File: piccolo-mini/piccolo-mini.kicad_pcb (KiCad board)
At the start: 2 copper layers, 96.1 x 20.6 mm, 16 parts, among them SW1 SW_Push, U1 ProMicro

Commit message: Continued tweaks
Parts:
- D1, D2, D3, D4, D5: footprint Keebio-Parts:Diode-Hybrid-Back -> Envoy:Diode-Hybrid-Back; moved to B.Cu
- MX1, MX2, MX3, MX4, MX5: footprint kbd:CherryMX_Hotswap -> Envoy:MXOnly-1U-Hotswap
- RESET1: renamed from SW1; footprint kbd:ResetSW -> Envoy:Reset_Jumper_Points
- U1: footprint Envoy:ProMicro_v3 -> Envoy:ProMicro_face_out; moved to B.Cu
- moved D3 3.12 mm to (192.4, 86.3)
- moved U1 1.00 mm to (151.7, 88.8), turned to -90 degrees
- moved D1 0.60 mm to (152.4, 88.2)
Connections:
- U1 pad 1: Net-(U1-Pad1) -> unconnected-(U1-Pad1)
- U1 pad 11: Net-(U1-Pad11) -> unconnected-(U1-Pad11)
- U1 pad 16: Net-(U1-Pad16) -> unconnected-(U1-Pad16)
- U1 pad 17: Net-(U1-Pad17) -> unconnected-(U1-Pad17)
- U1 pad 18: Net-(U1-Pad18) -> unconnected-(U1-Pad18)
- U1 pad 19: Net-(U1-Pad19) -> unconnected-(U1-Pad19)
- U1 pad 2: Net-(U1-Pad2) -> unconnected-(U1-Pad2)
- U1 pad 20: Net-(U1-Pad20) -> unconnected-(U1-Pad20)
- U1 pad 24: Net-(U1-Pad24) -> unconnected-(U1-Pad24)
- U1 pad 5: Net-(U1-Pad5) -> unconnected-(U1-Pad5)
- U1 pad 6: Net-(U1-Pad6) -> unconnected-(U1-Pad6)
- U1 pad 7: Net-(U1-Pad7) -> unconnected-(U1-Pad7)
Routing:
- net col0: track 63.5 -> 72.6 mm
- net GND: track 101.6 -> 107.7 mm
- net row0: track 40.8 -> 44.3 mm
- net row1: track 67.5 -> 70.9 mm, vias 2 -> 1
- net col2: track 19.2 -> 17.1 mm
- net Net-(D3-Pad2): track 3.38 -> 5.30 mm
- net col1: track 73.9 -> 74.9 mm
- net EncoderA: track 53.9 -> 54.6 mm
- net Reset: track 36.6 -> 37.2 mm
- net EncoderB: track 63.0 -> 62.6 mm, vias 2 -> 0
- added copper zone on B.Cu, net GND
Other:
- board size 96.1 x 20.6 mm -> 96.9 x 20.6 mm
- net class Default removed
- net class Power removed

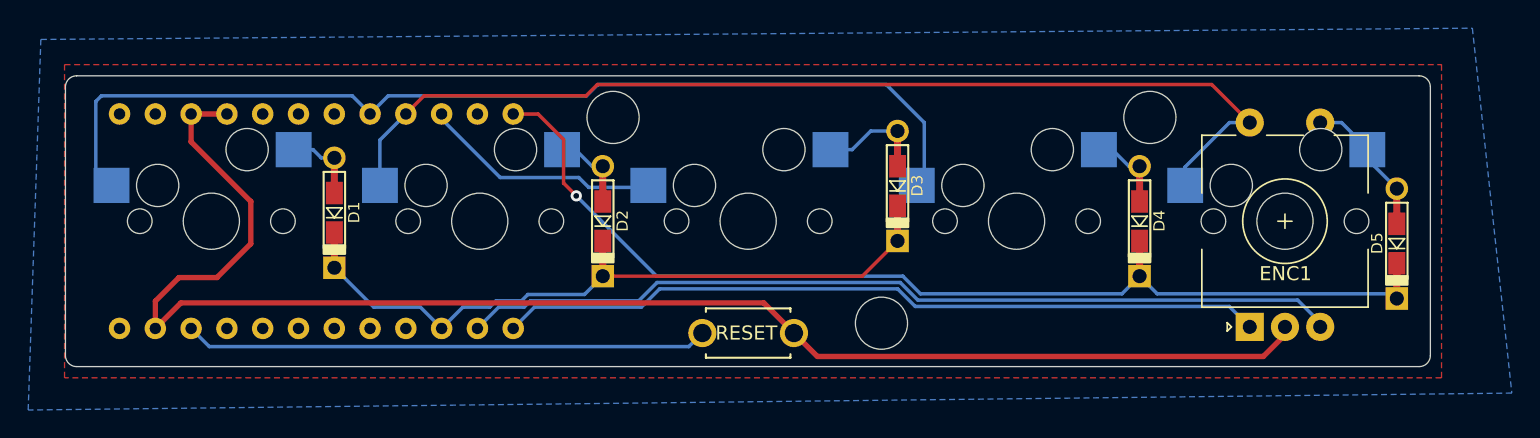
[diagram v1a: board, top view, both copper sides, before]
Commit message: Big re-route on piccolo mini to get diodes onto the back and out of the way
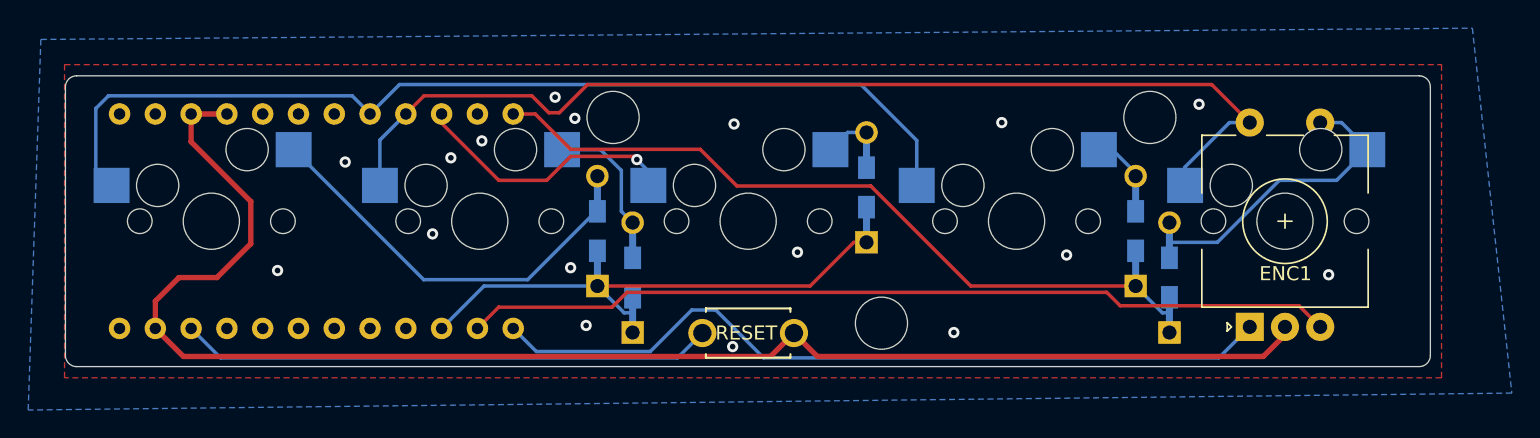
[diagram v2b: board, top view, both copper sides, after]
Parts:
- D1, D2, D3, D4, D5: moved to F.Cu
- moved D1 18.7 mm to (171.1, 89.5)
- moved D5 16.3 mm to (211.7, 92.8)
- moved D2 4.53 mm to (173.6, 92.8)
- moved D3 2.20 mm to (190.2, 86.4)
- moved D4 0.75 mm to (209.3, 89.5)
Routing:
- net Net-(D1-Pad2): track 3.13 -> 28.4 mm
- net row1: track 70.9 -> 52.4 mm, vias 1 -> 0
- net Net-(D5-Pad2): track 7.83 -> 21.0 mm
- net row0: track 44.3 -> 36.3 mm
- net Net-(D2-Pad2): track 3.38 -> 8.85 mm
- net Net-(D3-Pad2): track 5.30 -> 3.06 mm
- net col2: track 17.1 -> 19.2 mm, vias 0 -> 1
- net EncoderA: track 54.6 -> 56.5 mm
- net col0: track 72.6 -> 70.8 mm
- net col1: track 74.9 -> 75.9 mm
- net EncoderB: track 62.6 -> 61.9 mm
- net Reset: track 37.2 -> 37.9 mm
- net GND: track 107.7 -> 107.5 mm, vias 0 -> 17
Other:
- board text added: "Piccolo Mini by JeJeff rev 0.1"

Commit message: rev0.1 pcb sent for prototype manufacturing
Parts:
- moved D1 19.0 mm to (152.2, 88.4)
- moved D2 3.58 mm to (171.0, 90.3)
- moved U1 0.52 mm to (151.7, 88.3)
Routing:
- net Net-(D1-Pad2): track 28.4 -> 2.93 mm
- net row0: track 36.3 -> 41.9 mm
- net col2: track 19.2 -> 24.1 mm
- net Net-(D2-Pad2): track 8.85 -> 6.18 mm
- net GND: track 107.5 -> 104.9 mm, vias 17 -> 2
- net Net-(D5-Pad2): track 21.0 -> 23.4 mm
- net EncoderB: track 61.9 -> 63.0 mm
- net col0: track 70.8 -> 71.7 mm
- net col1: track 75.9 -> 75.2 mm
- net row1: track 52.4 -> 52.6 mm, vias 0 -> 1
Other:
- board text added: "JLCJLCJLCJLC"

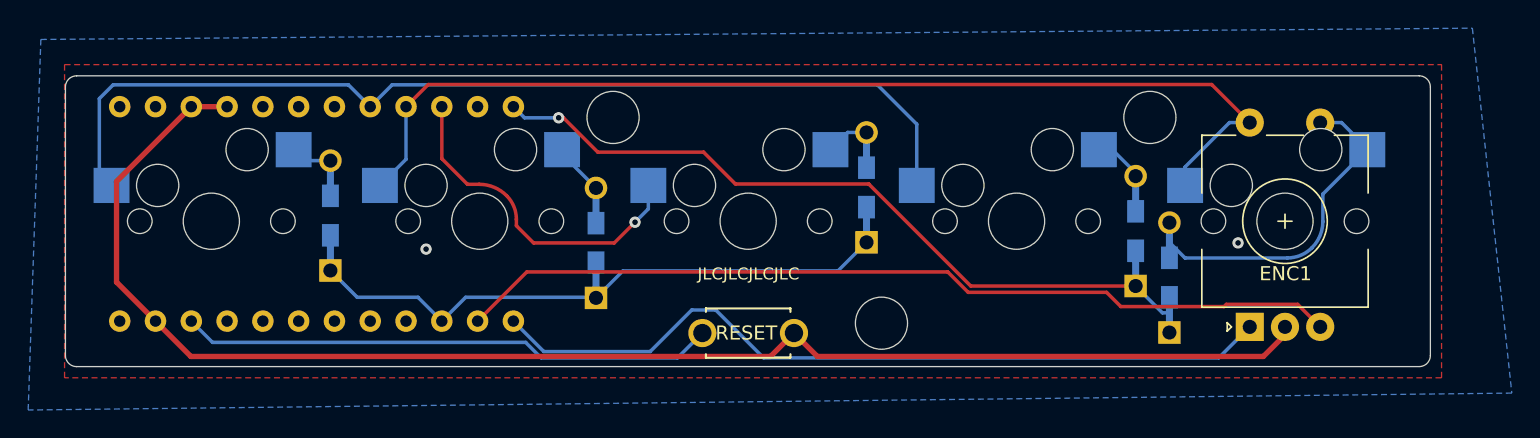
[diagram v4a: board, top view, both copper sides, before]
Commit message: Remove a few pro micro pins that get in the way
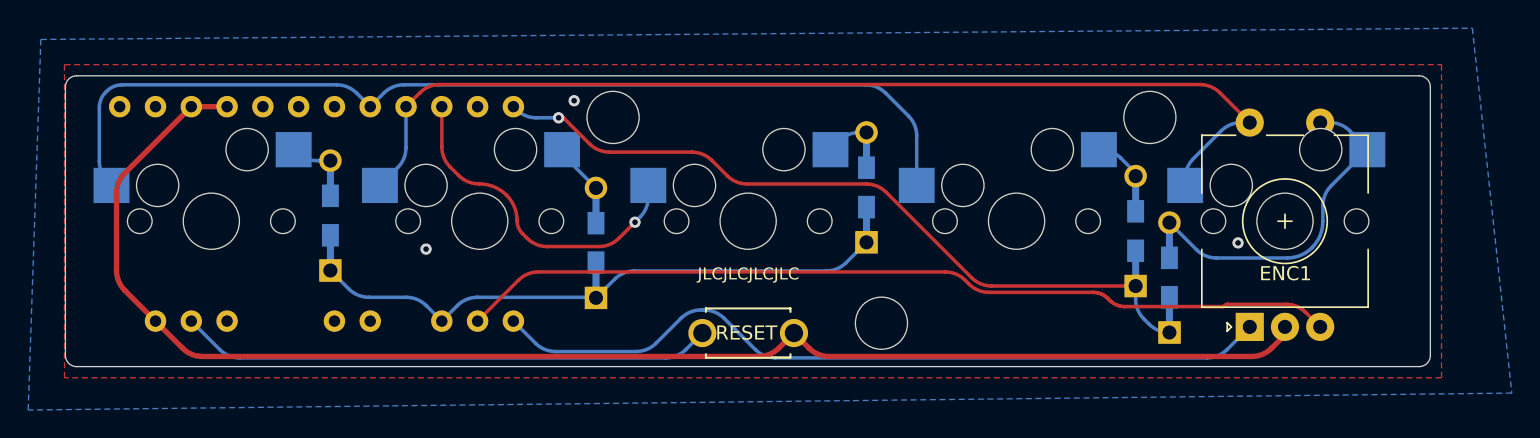
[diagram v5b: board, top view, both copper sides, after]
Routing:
- net row1: track 52.6 -> 53.5 mm
- net col0: track 71.7 -> 71.1 mm
- net GND: track 104.9 -> 104.4 mm, vias 2 -> 3
- net EncoderA: track 56.7 -> 56.1 mm
- net EncoderB: track 63.0 -> 62.5 mm
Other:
- board text added: "Piccolo Mini by JeJeff rev 0.2"
- board text added: "Pin 23 - GND is partially obstructed by a keyswitch and should be shortened in the pin header to barely protrude from the PCB"
- board text added: "The following unused pins are obstructed by a key switch 24 - RAW 20 - A3/PF4 19 - A2/PF5 16 - 15/PB1 These pins should be removed from the pin header"
- board text removed: "Piccolo Mini by JeJeff rev 0.1"
